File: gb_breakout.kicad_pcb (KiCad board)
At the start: 2 copper layers, 51 x 60.7 mm, 13 parts, among them J1 Conn_02x16_Odd_Even, U1 Cartridge_Bus

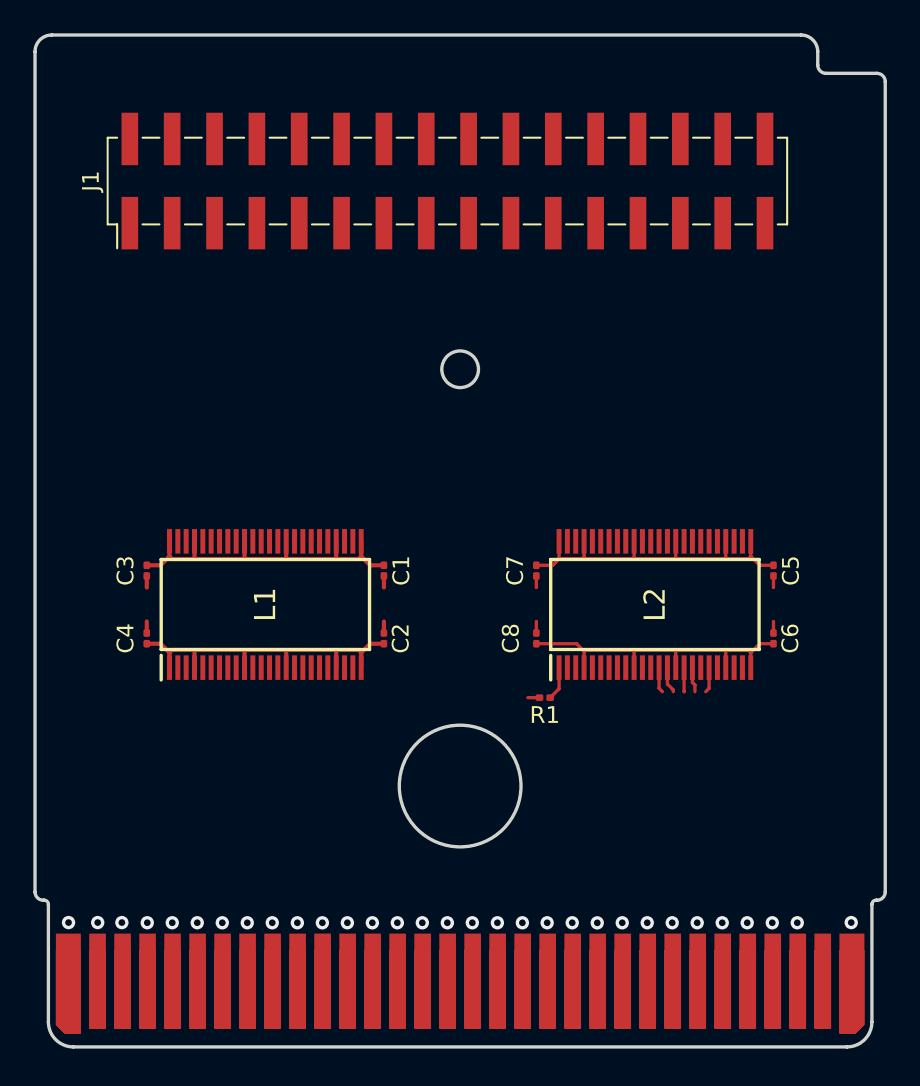
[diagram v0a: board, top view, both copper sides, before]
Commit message: add libs + fix associations
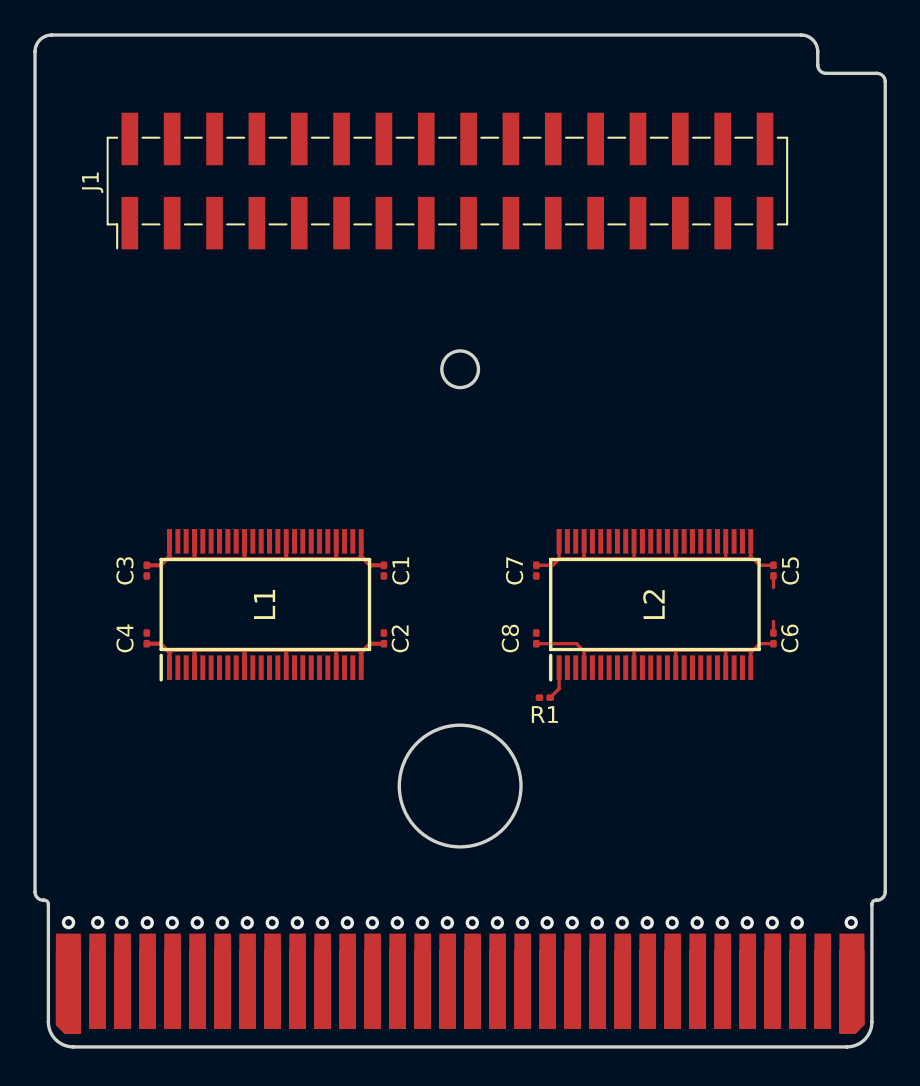
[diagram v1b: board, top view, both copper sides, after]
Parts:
- J1: value Conn_02x16_Odd_Even -> Conn_02x16_Counter_Clockwise
- L1, L2: footprint SamacSys_Parts:SOP50P810X120-48N -> 74ACT16245DGGR:SOP50P810X120-48N
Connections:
- J1 pad 10: BO_~{CS} -> BO_A9
- J1 pad 11: BO_A5 -> BO_A10
- J1 pad 12: BO_D0 -> BO_A11
- J1 pad 13: BO_A6 -> BO_A12
- J1 pad 14: BO_D1 -> BO_A13
- J1 pad 15: BO_A7 -> BO_A14
- J1 pad 16: BO_D2 -> BO_A15
- J1 pad 17: BO_A8 -> GND
- J1 pad 18: BO_D3 -> +3V3
- J1 pad 19: BO_A9 -> BO_~{RST}
- J1 pad 2: +5V -> BO_A1
- J1 pad 20: BO_D4 -> BO_D7
- J1 pad 21: BO_A10 -> BO_D6
- J1 pad 23: BO_A11 -> BO_D4
- J1 pad 24: BO_D6 -> BO_D3
- J1 pad 25: BO_A12 -> BO_D2
- J1 pad 26: BO_D7 -> BO_D1
- J1 pad 27: BO_A13 -> BO_D0
- J1 pad 28: BO_~{RST} -> BO_~{CS}
- J1 pad 29: BO_A14 -> BO_~{RD}
- J1 pad 3: BO_A1 -> BO_A2
- J1 pad 30: +3V3 -> BO_~{WR}
- J1 pad 31: BO_A15 -> BO_CLK
- J1 pad 32: GND -> +5V
- J1 pad 4: BO_CLK -> BO_A3
- J1 pad 5: BO_A2 -> BO_A4
- J1 pad 6: BO_~{WR} -> BO_A5
- J1 pad 7: BO_A3 -> BO_A6
- J1 pad 8: BO_~{RD} -> BO_A7
- J1 pad 9: BO_A4 -> BO_A8
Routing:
- net +5V: track 6.26 -> 1.39 mm
- net GB_~{WR}: track 3.61 -> 2.02 mm
- net GB_CLK: track 1.53 -> 0.00 mm
- net GB_~{RST}: track 1.52 -> 0.00 mm
- net GB_~{CS}: track 1.50 -> 0.00 mm
- net GB_~{RD}: track 1.44 -> 0.00 mm

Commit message: finished power+gnd routing
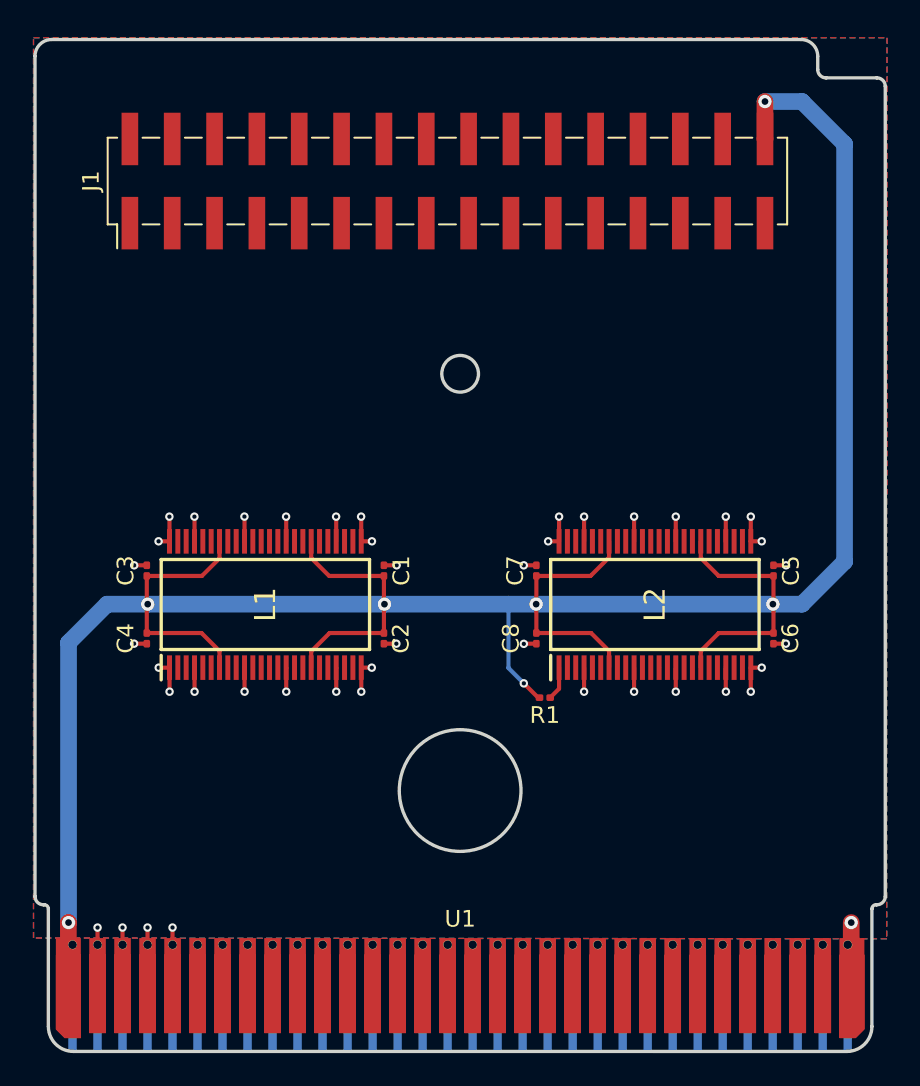
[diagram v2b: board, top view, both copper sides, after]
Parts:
- moved U1 0.27 mm to (142.2, 119.4)
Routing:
- net +5V: track 1.39 -> 166.6 mm, vias 1 -> 7
- net GND: track 82.5 -> 45.9 mm, vias 1 -> 39
- net GB_CLK: track 0.00 -> 1.04 mm
- net GB_~{WR}: track 2.02 -> 3.06 mm
- net GB_~{CS}: track 0.00 -> 1.03 mm
- net GB_~{RD}: track 0.00 -> 1.03 mm
- net GB_~{RST}: vias 1 -> 0
- net GB_D7: vias 1 -> 0
- net GB_D6: vias 1 -> 0
- net GB_D5: vias 1 -> 0
- net GB_D4: vias 1 -> 0
- net GB_D3: vias 1 -> 0
- net GB_D2: vias 1 -> 0
- net GB_D1: vias 1 -> 0
- net GB_D0: vias 1 -> 0
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- added copper zone on B.Cu, net GND
- added copper zone on F.Cu, net GND
